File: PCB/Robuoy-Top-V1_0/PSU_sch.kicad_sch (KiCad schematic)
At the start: 47 parts, among them J1 Accu, J5 Power/On_Off, Q1 FS8205A, Q2 A03401A, U1 TP4056, U7 TLV61046ADB, U8 TLV61046ADB

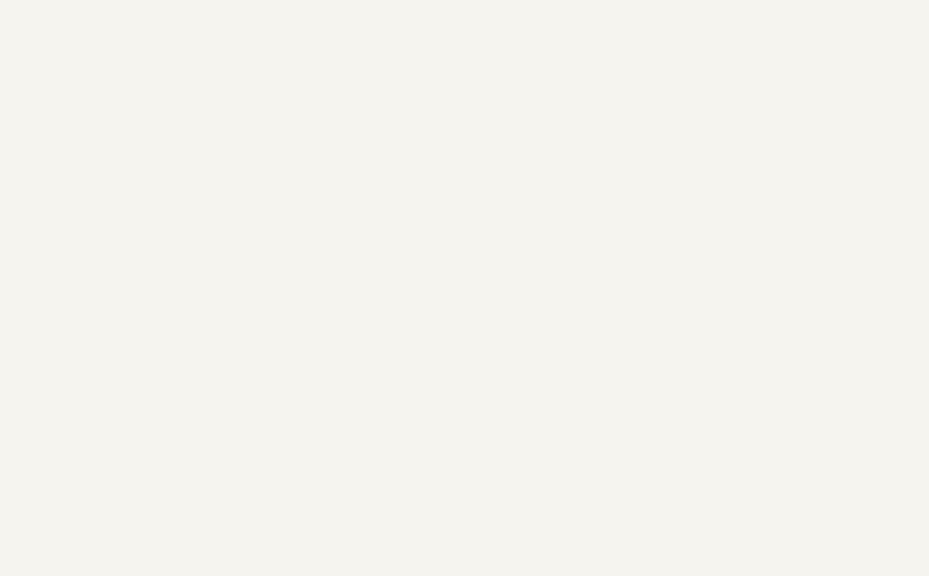
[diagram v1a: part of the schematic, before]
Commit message: Sub ready for routing
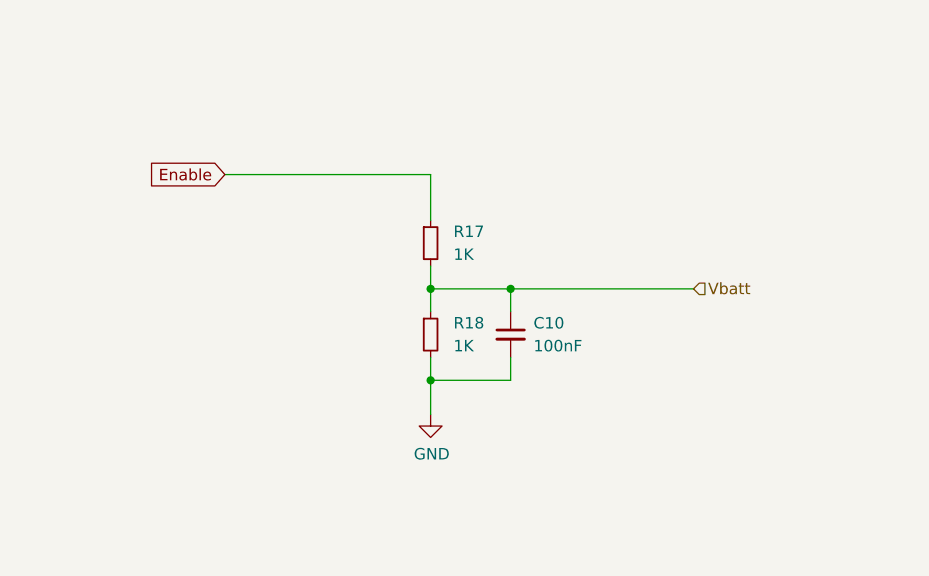
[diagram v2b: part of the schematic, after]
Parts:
- added C10: 100nF, symbol Device:C_Small
- added R17, R18: 1K, A_Device:R_0603, symbol Device:R_Small
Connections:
- net Enable: now also R17.1
- net GND: now also C10.2, R18.2
- new net Vbatt: C10.1, R17.2, R18.1

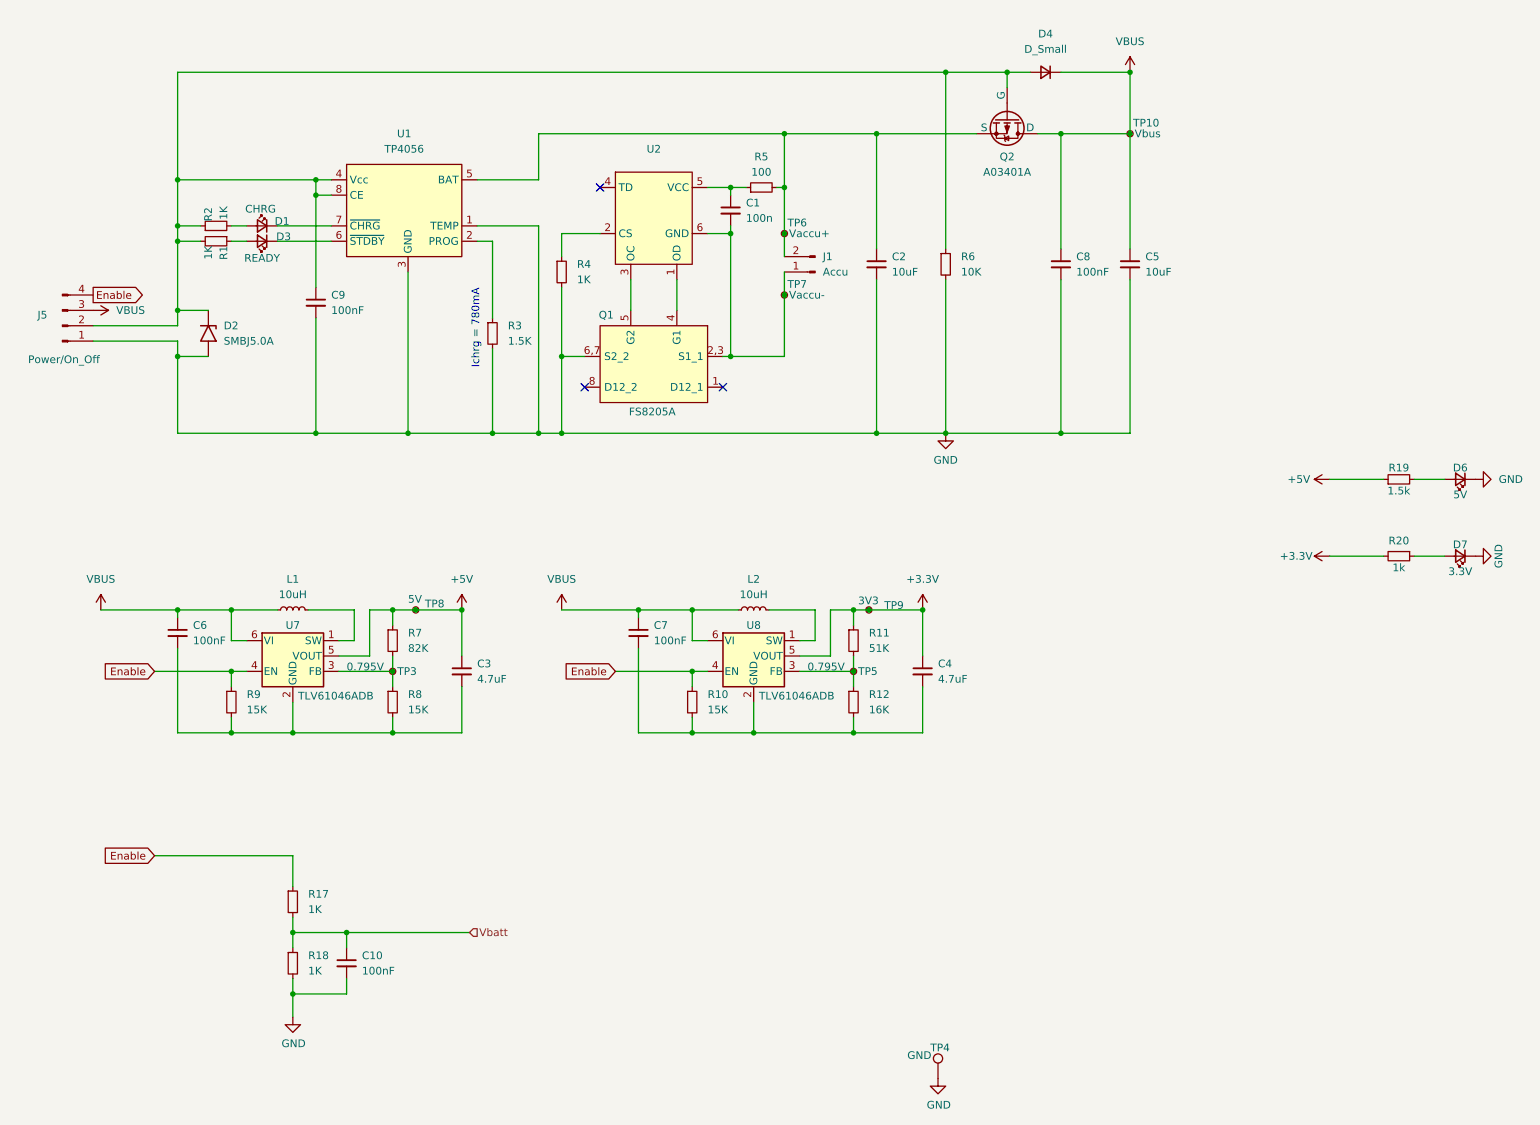
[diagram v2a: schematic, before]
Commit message: Pcb's getting ready for routing
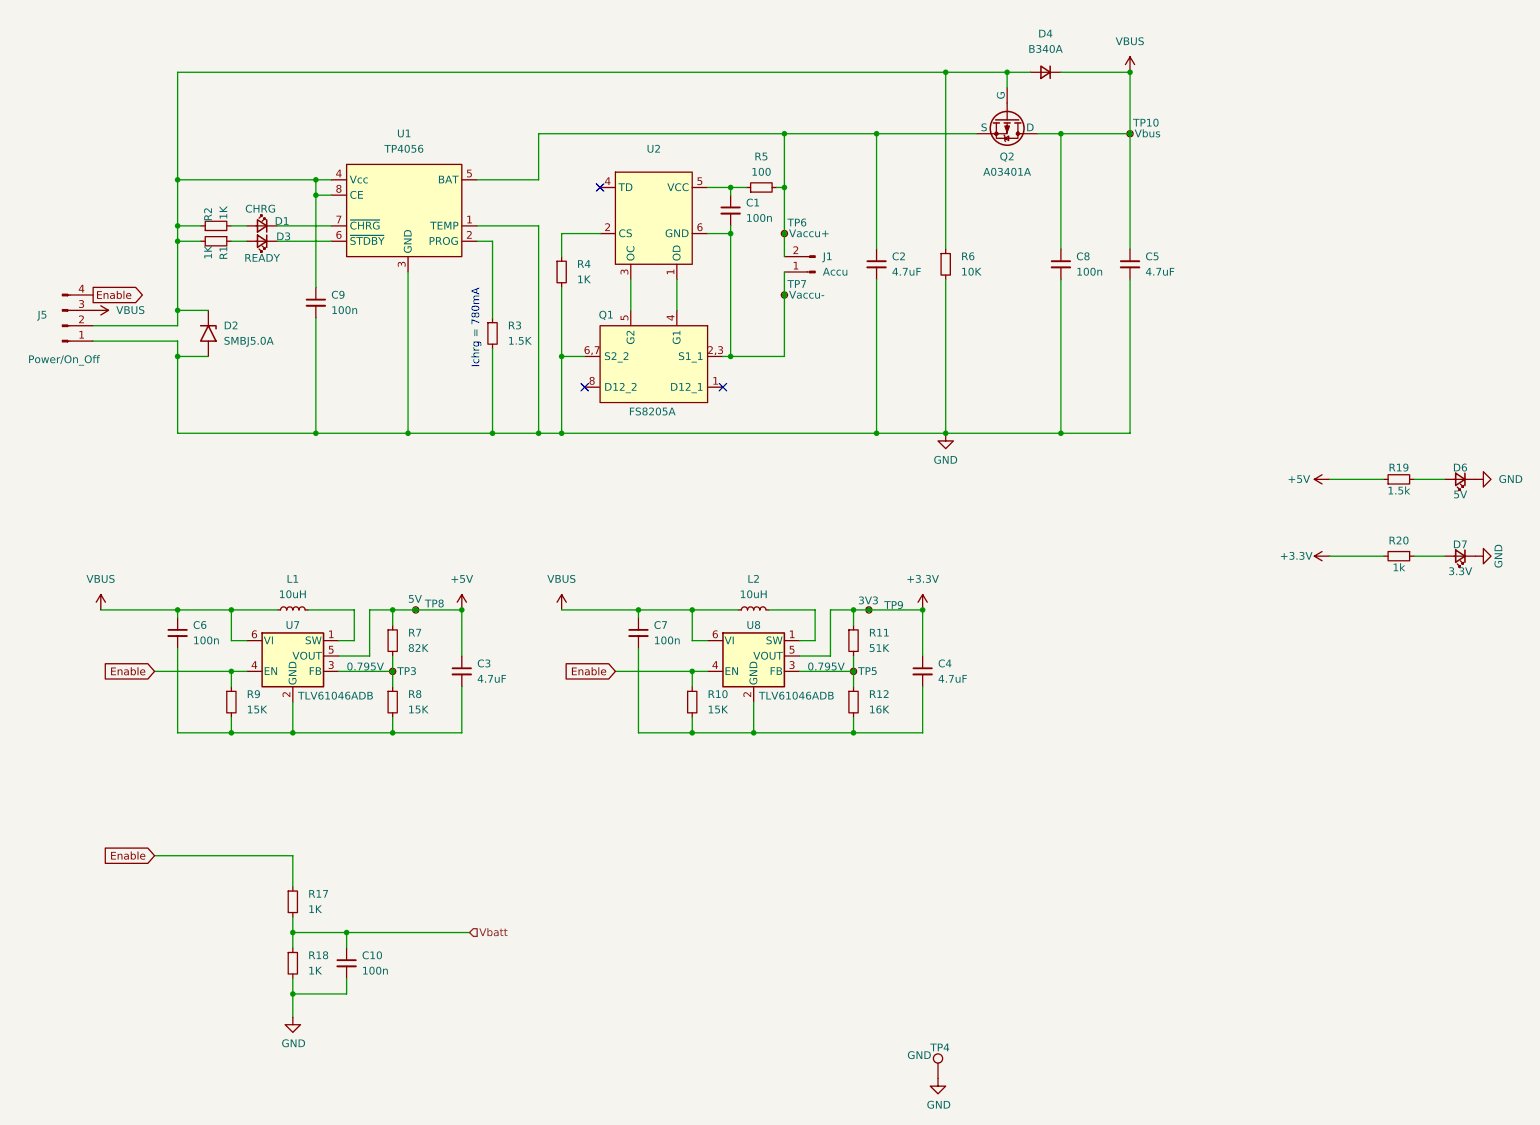
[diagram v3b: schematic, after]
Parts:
- C1: footprint (none) -> A_Device:C_0603; LCSC (none) -> C14663
- C10, C6, C7, C8, C9: value 100nF -> 100n; footprint (none) -> A_Device:C_0603; LCSC (none) -> C14663
- C2, C5: value 10uF -> 4.7uF; footprint (none) -> A_Device:C_1206_(1.6); LCSC (none) -> C29823
- C3, C4: footprint (none) -> A_Device:C_1206_(1.6); LCSC (none) -> C29823
- D3: footprint (none) -> A_Device:LED_0603; LCSC (none) -> C2286
- D4: value D_Small -> B340A; footprint (none) -> Diode_SMD:D_SMA; LCSC (none) -> C85098
- D6, D7: footprint LED_SMD:LED_0603_1608Metric -> A_Passive:LED_0805; LCSC C72043 -> C2297

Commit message: gETTING READY FOR ROUTING
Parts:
- added TP203: Vbatt, A_Pads_Pins:Testpad_2, symbol Connector:TestPoint_Small
- D202: renamed from D1; footprint (none) -> A_Device:LED_0603; LCSC (none) -> C2286
- D203: renamed from D3; footprint A_Device:LED_0603 -> A_Device:LED_0805; LCSC C2286 -> C2297
- D6, D7: footprint A_Passive:LED_0805 -> A_Device:LED_0805
- J201: renamed from J5; footprint (none) -> Connector_JST:JST_XH_B4B-XH-A_1x04_P2.50mm_Vertical; LCSC (none) -> C5341203
- J202: renamed from J1; footprint (none) -> A_Connector:Header_1x02_P2.54_Male; LCSC (none) -> C492401
- L201: renamed from L1; footprint (none) -> A_Device:FTC252012S
- L202: renamed from L2; footprint (none) -> A_Device:FTC252012S
- Q201: renamed from Q1; LCSC (none) -> C2830320
- Q202: renamed from Q2; footprint (none) -> Package_TO_SOT_SMD:SOT-23
- R19: value 1.5k -> 1.5K
- R20: value 1k -> 1K
- R203: renamed from R9; footprint (none) -> A_Device:R_0603; LCSC (none) -> C21190
- R206: renamed from R7; footprint (none) -> A_Device:R_0603
- R207: renamed from R8; footprint (none) -> A_Device:R_0603
- R210: renamed from R10; footprint (none) -> A_Device:R_0603
- R211: renamed from R5; LCSC (none) -> C22775
- R212: renamed from R11; footprint (none) -> A_Device:R_0603
- R213: renamed from R12; footprint (none) -> A_Device:R_0603
- TP201: renamed from TP3; footprint (none) -> A_Pads_Pins:Testpad_2; now left out of the parts list
- TP202: renamed from TP8; footprint (none) -> A_Pads_Pins:Testpoint_0.9x1.5
- TP204: renamed from TP6; footprint (none) -> A_Pads_Pins:Testpad_2
- TP205: renamed from TP7; footprint (none) -> A_Pads_Pins:Testpad_2
- TP206: renamed from TP5; footprint (none) -> A_Pads_Pins:Testpad_2; now left out of the parts list
- TP207: renamed from TP9; footprint (none) -> A_Pads_Pins:Testpad_2
- TP209: renamed from TP10; footprint (none) -> A_Pads_Pins:Testpad_2; now left out of the parts list
- U201: renamed from U7; LCSC (none) -> C464815
- U203: renamed from U2; value ~ -> DW01A
- U204: renamed from U8; LCSC (none) -> C464815
- renumbered C6 to C201, C9 to C202, C10 to C203, C3 to C204, C7 to C205, C1 to C206, C2 to C207, C4 to C208, C8 to C209, C5 to C210, D2 to D201, D4 to D204, R2 to R201, R1 to R202, R17 to R204, R18 to R205, R3 to R208, R4 to R209, R6 to R214, U1 to U202
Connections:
- net Vbatt: now also TP203.1

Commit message: Some more routing
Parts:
- removed R203, R210: 15K, A_Device:R_0603, symbol Device:R_Small
- Q201: footprint SOP65P640X120-8N -> Package_SO:TSSOP-8_4.4x3mm_P0.65mm
- TP201, TP203, TP204, TP205, TP206, TP207, TP209: footprint A_Pads_Pins:Testpad_2 -> A_Pads_Pins:Testpad_1.4
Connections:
- net GND: now also C201.2, C204.2, C205.2, C208.2, Q201.6 (S2_2), Q201.7 (S2_2), R207.2, R213.2, U201.2 (GND), U204.2 (GND); no longer Q201.6,7 (S2_2)
- net PAD: now reaches C202.1, D201.1 (A1), D204.2 (A), J201.2 (Pin_2), Q202.2 (G), R201.1, R202.2, R214.1, U202.4 (Vcc), U202.8 (CE)
- net PAD: now also U202.9 (PAD)
- net at C206.2, J202.1 (Pin_1), TP205.1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: now also Q201.2 (S1_1), Q201.3 (S1_1); no longer Q201.2,3 (S1_1)

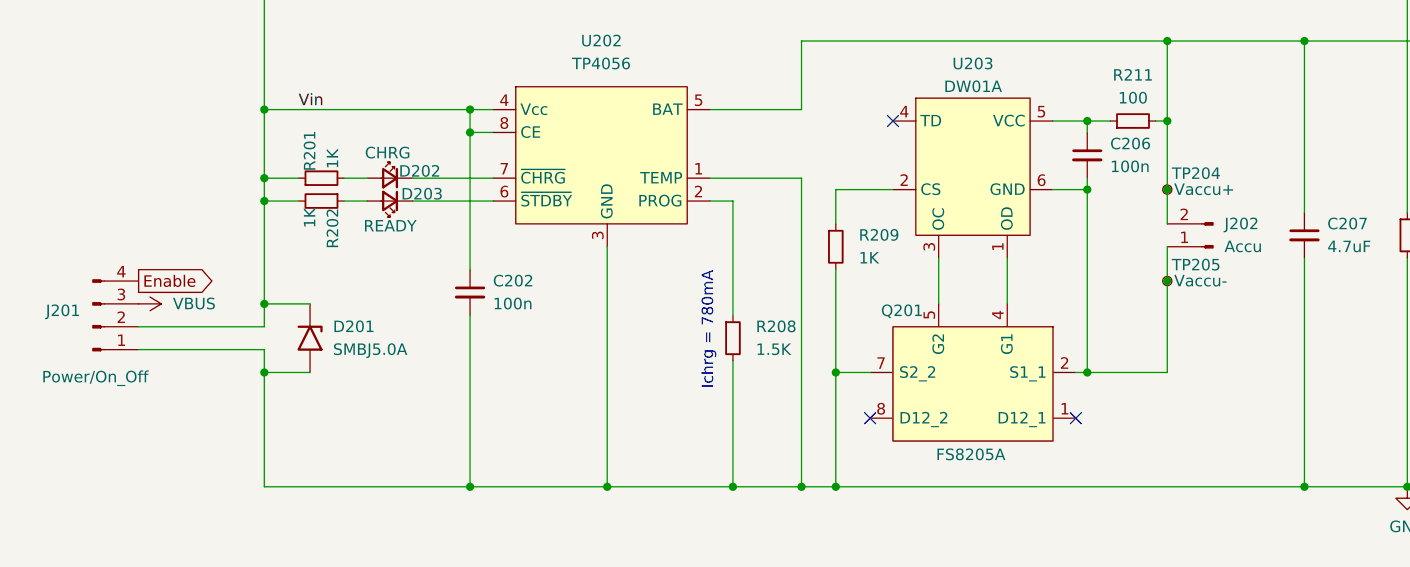
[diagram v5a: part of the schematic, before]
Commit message: Top Pcb finished Botom Cup finished
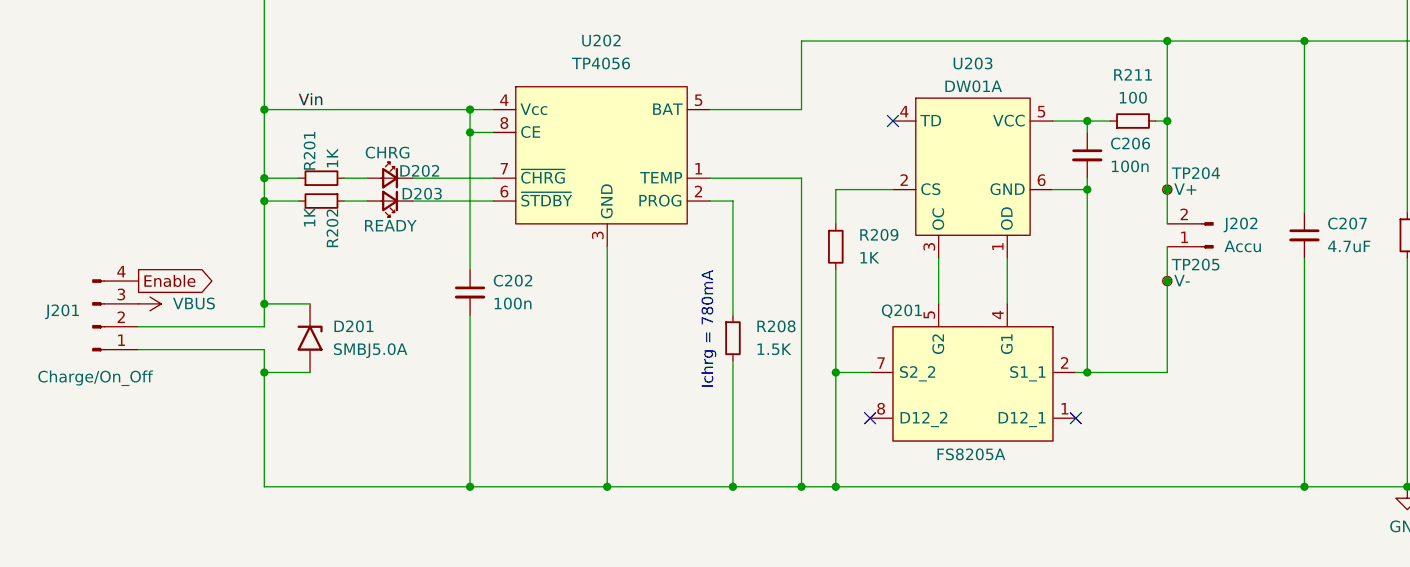
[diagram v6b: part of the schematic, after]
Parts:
- J201: value Power/On_Off -> Charge/On_Off
- TP202, TP207, TP4: now left out of the parts list
- TP204: value Vaccu+ -> V+; now left out of the parts list
- TP205: value Vaccu- -> V-; now left out of the parts list
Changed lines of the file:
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@@
 		(unit 1)
 		(exclude_from_sim no)
-		(in_bom yes)
+		(in_bom no)
 		(on_board yes)
 		(dnp no)
@@
 			)
 		)
-		(property "Value" "Vaccu-"
+		(property "Value" "V-"
 			(at 145.542 59.69 0)
 			(effects
@@
 		(unit 1)
 		(exclude_from_sim no)
-		(in_bom yes)
+		(in_bom no)
 		(on_board yes)
 		(dnp no)
@@
 		(unit 1)
 		(exclude_from_sim no)
-		(in_bom yes)
+		(in_bom no)
 		(on_board yes)
 		(dnp no)
@@
 		(unit 1)
 		(exclude_from_sim no)
-		(in_bom yes)
+		(in_bom no)
 		(on_board yes)
 		(dnp no)
@@
 			)
 		)
-		(property "Value" "Power/On_Off"
+		(property "Value" "Charge/On_Off"
 			(at 25.654 70.358 0)
 			(effects
@@
 		(unit 1)
 		(exclude_from_sim no)
-		(in_bom yes)
+		(in_bom no)
 		(on_board yes)
 		(dnp no)
@@
 			)
 		)
-		(property "Value" "Vaccu+"
+		(property "Value" "V+"
 			(at 145.542 49.53 0)
 			(effects

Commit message: PCB changed
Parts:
- added R203: 15K, A_Device:R_0603, symbol Device:R_Small
- added SW202: SS-12D11-G050/On-Off, A_Connector:SS-12D10L5, symbol Switch:SW_DPST_x2
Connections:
- net Enable: now also R203.1, SW202.2 (B)
- net GND: now also R203.2
- net VBUS: now also SW202.1 (A)

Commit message: PCB changed
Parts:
- removed SW202: SS-12D11-G050/On-Off, A_Connector:SS-12D10L5, symbol Switch:SW_DPST_x2
- added SW201: On/Off, A_Connector:SS-12D10L5, symbol NicE:SW_slide_SP
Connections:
- net Enable: now also SW201.2
- net VBUS: now also SW201.1
- no-connect marks 3 -> 4
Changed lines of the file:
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@@
 	)
 	(no_connect
+		(at 224.79 20.32)
+	)
+	(no_connect
 		(at 134.62 74.93)
 	)
@@
 	(wire
 		(pts
+			(xy 219.71 20.32) (xy 219.71 22.86)
+		)
+		(stroke
+			(width 0)
+			(type default)
+		)
+	)
+	(wire
+		(pts
 			(xy 107.95 49.53) (xy 107.95 53.34)
 		)
@@
 	(wire
 		(pts
+			(xy 214.63 20.32) (xy 214.63 22.86)
+		)
+		(stroke
+			(width 0)
+			(type default)
+		)
+	)
+	(wire
+		(pts
 			(xy 190.5 33.02) (xy 190.5 52.07)
 		)
@@
 	(wire
 		(pts
+			(xy 219.71 22.86) (xy 229.87 22.86)
+		)
+		(stroke
+			(width 0)
+			(type default)
+		)
+	)
+	(wire
+		(pts
 			(xy 63.5 152.4) (xy 63.5 157.48)
 		)
@@
 	(wire
 		(pts
-			(xy 229.87 22.86) (xy 224.79 22.86)
-		)
-		(stroke
-			(width 0)
-			(type default)
-		)
-	)
-	(wire
-		(pts
 			(xy 44.45 62.23) (xy 49.53 62.23)
 		)
@@
 	)
 	(symbol
+		(lib_id "NicE:SW_slide_SP")
+		(at 219.71 17.78 90)
+		(unit 1)
+		(exclude_from_sim no)
+		(in_bom yes)
+		(on_board yes)
+		(dnp no)
+		(property "Reference" "SW201"
+			(at 217.17 24.384 90)
+			(effects
+				(font
+					(size 1.27 1.27)
+				)
+			)
+		)
+		(property "Value" "On/Off"
+			(at 217.17 14.224 90)
+			(effects
+				(font
+					(size 1.27 1.27)
+				)
+			)
+		)
+		(property "Footprint" "A_Connector:SS-12D10L5"
+			(at 219.71 15.24 0)
+			(effects
+				(font
+					(size 1.27 1.27)
+				)
+				(hide yes)
+			)
+		)
+		(property "Datasheet" ""
+			(at 219.71 15.24 0)
+			(effects
+				(font
+					(size 1.27 1.27)
+				)
+				(hide yes)
+			)
+		)
+		(property "Description" ""
+			(at 219.71 15.24 0)
+			(effects
+				(font
+					(size 1.27 1.27)
+				)
+				(hide yes)
+			)
+		)
+		(property "LCSC" "C319012"
+			(at 219.71 17.78 0)
+			(effects
+				(font
+					(size 1.27 1.27)
+				)
+				(hide yes)
+			)
+		)
+		(pin "3"
+		)
+		(pin "2"
+		)
+		(pin "1"
+		)
+		(instances
+			(project "Robuoy-Top"
+				(path "/77bea089-a6ae-4a6f-b95b-7a9010ad7c5d/b4716c37-6296-4cc3-83d4-c08b9373ace7"
+					(reference "SW201")
+					(unit 1)
+				)
+			)
+		)
+	)
+	(symbol
 		(lib_id "Device:R_Small")
 		(at 50.8 48.26 90)
@@
 					(unit 1)
 				)
-			)
-		)
-	)
-	(symbol
-		(lib_id "Switch:SW_DPST_x2")
-		(at 219.71 22.86 0)
-		(unit 1)
-		(exclude_from_sim no)
-		(in_bom yes)
-		(on_board yes)
-		(dnp no)
-		(fields_autoplaced yes)
-		(property "Reference" "SW202"
-			(at 219.71 16.51 0)
-			(effects
-				(font
-					(size 1.27 1.27)
-				)
-			)
-		)
-		(property "Value" "SS-12D11-G050/On-Off"
-			(at 219.71 19.05 0)
-			(effects
-				(font
-					(size 1.27 1.27)
-				)
-			)
-		)
-		(property "Footprint" "A_Connector:SS-12D10L5"
-			(at 219.71 22.86 0)
-			(effects
-				(font
-					(size 1.27 1.27)
-				)
-				(hide yes)
-			)
-		)
-		(property "Datasheet" "https://wmsc.lcsc.com/wmsc/upload/file/pdf/v2/lcsc/2110151630_XKB-Connection-SS-12D10L5_C319012.pdf"
-			(at 219.71 22.86 0)
-			(effects
-				(font
-					(size 1.27 1.27)
-				)
-				(hide yes)
-			)
-		)
-		(property "Description" "Single Pole Single Throw (SPST) switch, separate symbol"
-			(at 219.71 22.86 0)
-			(effects
-				(font
-					(size 1.27 1.27)
-				)
-				(hide yes)
-			)
-		)
-		(property "LCSC" "C319012"
-			(at 219.71 22.86 90)
-			(effects
-				(font
-					(size 1.27 1.27)
-				)
-				(hide yes)
-			)
-		)
-		(pin "4"
-		)
-		(pin "2"
-		)
-		(pin "1"
-		)
-		(pin "3"
-		)
-		(instances
-			(project "Robuoy-Top"
-				(path "/77bea089-a6ae-4a6f-b95b-7a9010ad7c5d/b4716c37-6296-4cc3-83d4-c08b9373ace7"
-					(reference "SW202")
-					(unit 1)
-				)
